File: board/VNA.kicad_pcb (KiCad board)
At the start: 2 copper layers, 100 x 100 mm, 146 parts, among them J1 Conn_02x07_Odd_Even, J10 Conn_01x01, J11 Conn_01x01, J12 Conn_01x01, J13 Barrel_Jack, J16 USB_B, J17 Conn_01x04, J18 Conn_01x01, J19 Conn_01x01, J2 Conn_Coaxial, J20 Conn_01x01, J21 Conn_01x01, J8 Conn_01x01, J9 Conn_Coaxial, Q1 SS9018, U1 SI5351A, U10 SI5351A, U11 MicroSD_SPI_CD, U2 LM339, U3 SA612, U4 SA612, U5 SA612, U6 LM358, U7 LM358, U8 LM1117-3.3, U9 LM7805_TO220, Y1 27 MHz

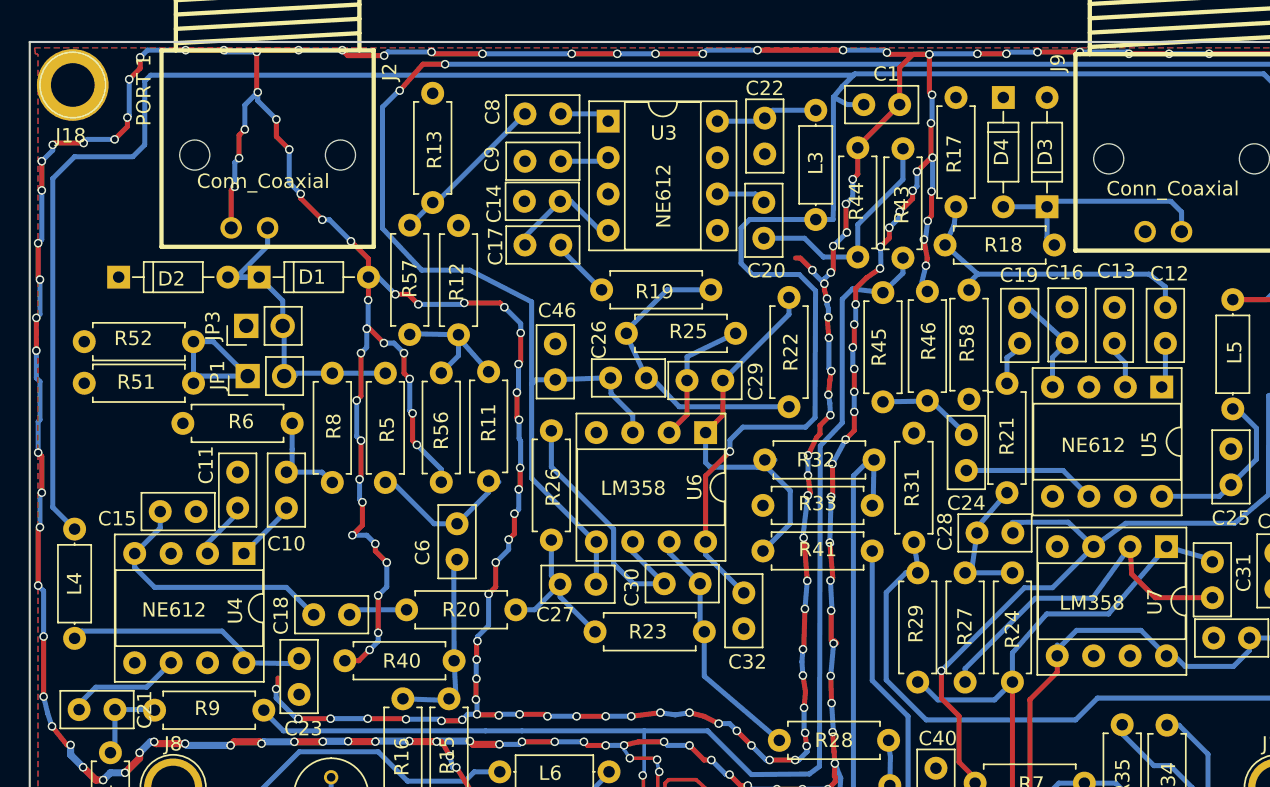
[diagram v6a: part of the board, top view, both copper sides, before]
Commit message: Modified some component values on bridge for better performance
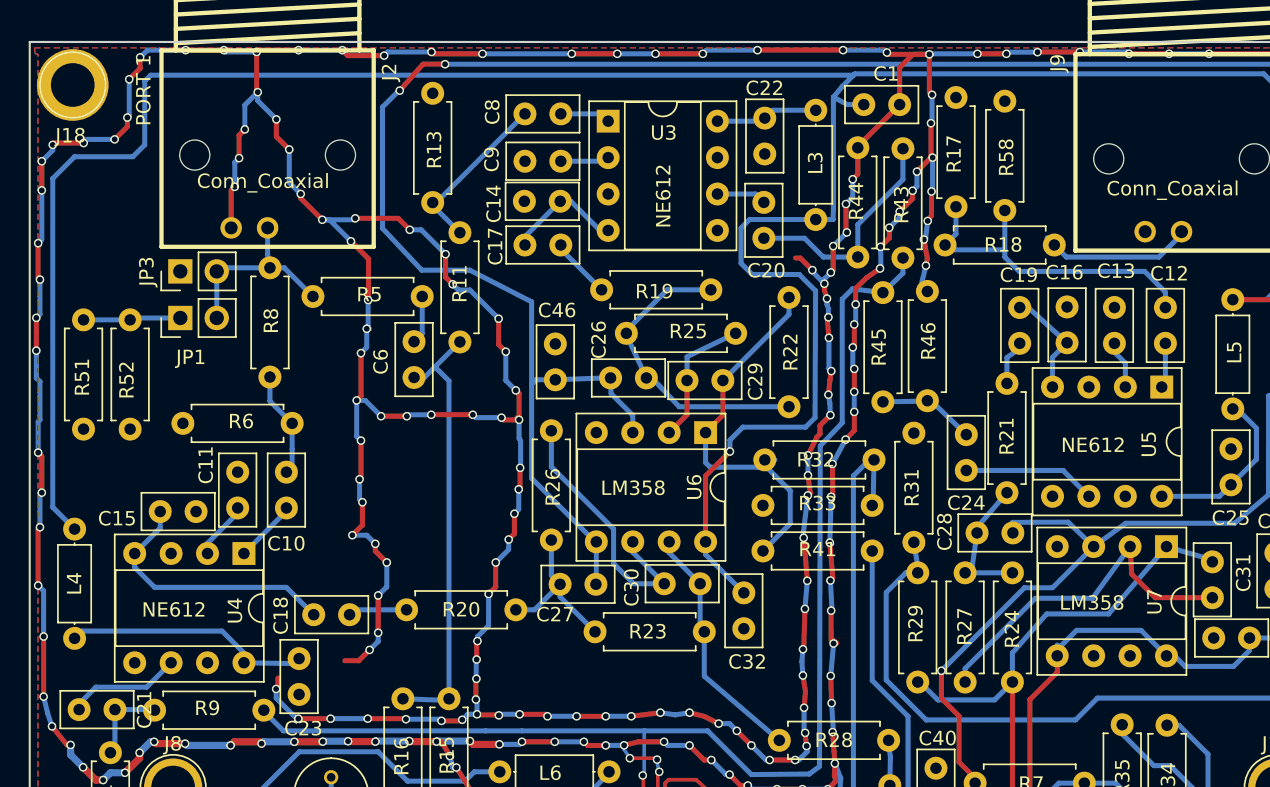
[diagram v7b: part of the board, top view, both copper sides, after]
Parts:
- removed D1, D2, D3, D4: 1N4148, Diodes_THT:D_DO-35_SOD27_P7.62mm_Horizontal
- removed R12, R40, R56: 100R, Resistors_THT:R_Axial_DIN0207_L6.3mm_D2.5mm_P7.62mm_Horizontal
- removed R57: 120R, Resistors_THT:R_Axial_DIN0207_L6.3mm_D2.5mm_P7.62mm_Horizontal
- R11: value 47R -> 82R
- R13, R6: value 4R7 -> 1R
- R15: value 220R -> 51R
- R18, R5: value 47R -> 51R
- R58: value 22R -> 1R
- moved C6 15.5 mm to (76.8, 70.9), turned to 270 degrees
- moved R11 9.90 mm to (80.0, 63.3)
- moved R8 8.54 mm to (66.8, 65.8)
- moved R5 7.36 mm to (69.8, 67.8), turned to 0 degrees
- moved R52 6.89 mm to (57.0, 77.0), turned to 90 degrees
- moved JP1 6.20 mm to (60.5, 69.2)
- moved R58 6.09 mm to (118.0, 61.8), turned to 90 degrees
- moved JP3 5.97 mm to (60.5, 66.0)
- moved R51 3.20 mm to (53.8, 77.0), turned to 90 degrees
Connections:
- R11 pad 1: Net-(R11-Pad1) -> SAMPVOLT
- R15 pad 1: Net-(C6-Pad1) -> CLK0
- R16 pad 1: Net-(C6-Pad1) -> CLK0
- R5 pad 2: CLK0 -> Net-(C6-Pad1)
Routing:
- net CLK0: track 12.1 -> 31.7 mm
- net Net-(J2-Pad1): track 23.8 -> 13.7 mm
- net Net-(R11-Pad1): track 9.95 -> 0.00 mm
- net Net-(C6-Pad1): track 13.3 -> 3.39 mm
- net Net-(J9-Pad1): track 17.5 -> 10.8 mm
- net Net-(JP1-Pad1): track 11.7 -> 6.80 mm
- net GND: track 603.6 -> 607.4 mm
- net SAMPCUR2: track 22.1 -> 23.8 mm
- net SAMPPORT: track 8.14 -> 7.44 mm
- net SAMPVOLT: track 11.3 -> 11.9 mm
